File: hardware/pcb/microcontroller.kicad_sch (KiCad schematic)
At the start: 46 parts, among them J3 GT-USB-7010ASV, J5 helios-pinout, Q1 2N7002VC-, Q2 2N7002VC-, SW18 SWITCH, U3 USBLC6-2P6, U4 TLV74333PDBVR, U5 W25Q128JVPIQ, U6 RP2040, U7 74LVC1T45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

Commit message: Version 2 sent to production
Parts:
- removed C9: 15p, Capacitor_SMD:C_0402_1005Metric, symbol Device:C
- removed FB1: 600R, Resistor_SMD:R_0402_1005Metric, symbol Device:FerriteBead_Small
- removed U4: TLV74333PDBVR, Package_TO_SOT_SMD:SOT-23-5, symbol 0xcb:LP5907SNX-3.3-NOPB
- removed U5: W25Q128JVPIQ, Package_SO:SOIC-8W_5.3x5.3mm_P1.27mm, symbol 0xcb:W25Q128JVPIQ
- added C21: 4.7u, Capacitor_SMD:C_0402_1005Metric, symbol Device:C
- added U1: W25Q64JV, Package_SON:WSON-8-1EP_8x6mm_P1.27mm_EP3.4x4.3mm, symbol Mathboard:W25Q64JV
- added U4: XC6206P332MR-G, Package_TO_SOT_SMD:SOT-23, symbol Mathboard:XC6206P332MR-G
- C2, C4, C5: value 10u -> 4.7u; LCSC C15525 -> C23733; MPN  10uF 20% 10V 0402 -> 4.7uF 20% 10V 0402
- C6: value 10u -> 30p; footprint Capacitor_SMD:C_0402_1005Metric -> Capacitor_SMD:C_0603_1608Metric; LCSC C15525 -> C1658; MPN  10uF 20% 10V 0402 -> 0603CG300J500NT
- C8: value 15p -> 30p; footprint Capacitor_SMD:C_0402_1005Metric -> Capacitor_SMD:C_0603_1608Metric; LCSC C1548 -> C1658; MPN  15pF 5% 10V -> 0603CG300J500NT
- D17: value PMEG2010BELD -> DSL14; footprint Diode_SMD:D_SOD-882D -> Diode_SMD:D_SOD-123; JLCPCB_CORRECTION 0; 0; 180 -> (none); LCSC C552820 -> C22466349; MPN  PMEG2010BELD,315 -> DSL14
- J3: value GT-USB-7010ASV -> TYPE-C sinking plate; footprint mathboard:USB_C_Receptacle_G-Switch_GT-USB-7010ASV -> mathboard:USB_C_Receptacle_XYECONN TYPE-C-F02C-1BBWC1.6; LCSC C2988369 -> C20883026; MPN  USB4510-03-1-A -> TYPE-C-F02C-1BBWC1.6
- R12, R13: footprint Resistor_SMD:R_0402_1005Metric -> Resistor_SMD:R_0603_1608Metric; LCSC C25100 -> C25190
- Y1: LCSC C2149204 -> C9002; MPN  ECS-120-10-36B-CWY-TR3 -> X322512MSB4SI
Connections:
- net +3V3: now also C5.1, U1.8 (VCC), U4.2 (VOUT); no longer C6.1
- net +5V: now also C21.1, U4.3 (VIN); no longer C5.1
- net GND: now also C2.1, C6.1, J3.S1 (SHIELD), C21.2, U1.4 (GND), U1.9 (EP), U4.1 (VSS); no longer C2.2, C6.2
- net QSPI_CLK: now also U1.6 (CLK)
- net QSPI_CS: now also U1.1 (~{CS})
- net QSPI_SD0: now also U1.5 (DI(IO0))
- net QSPI_SD1: now also U1.2 (DO(IO1))
- net QSPI_SD2: now also U1.3 (IO2)
- net QSPI_SD3: now also U1.7 (IO3)
- net VBUS: now also C2.2; no longer C2.1
- net at R14.1, Y1.1: now also C6.2
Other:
- moved on the sheet: C7

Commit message: Revision 4
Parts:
- U1: footprint Package_SON:WSON-8-1EP_8x6mm_P1.27mm_EP3.4x4.3mm -> mathboard:WSON-8-1EP_8x6mm_P1.27mm_EP3.4x4.3mm
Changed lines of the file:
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@@
 			)
 		)
-		(property "Footprint" "Package_SON:WSON-8-1EP_8x6mm_P1.27mm_EP3.4x4.3mm"
+		(property "Footprint" "mathboard:WSON-8-1EP_8x6mm_P1.27mm_EP3.4x4.3mm"
 			(at 134.874 73.152 0)
 			(effects

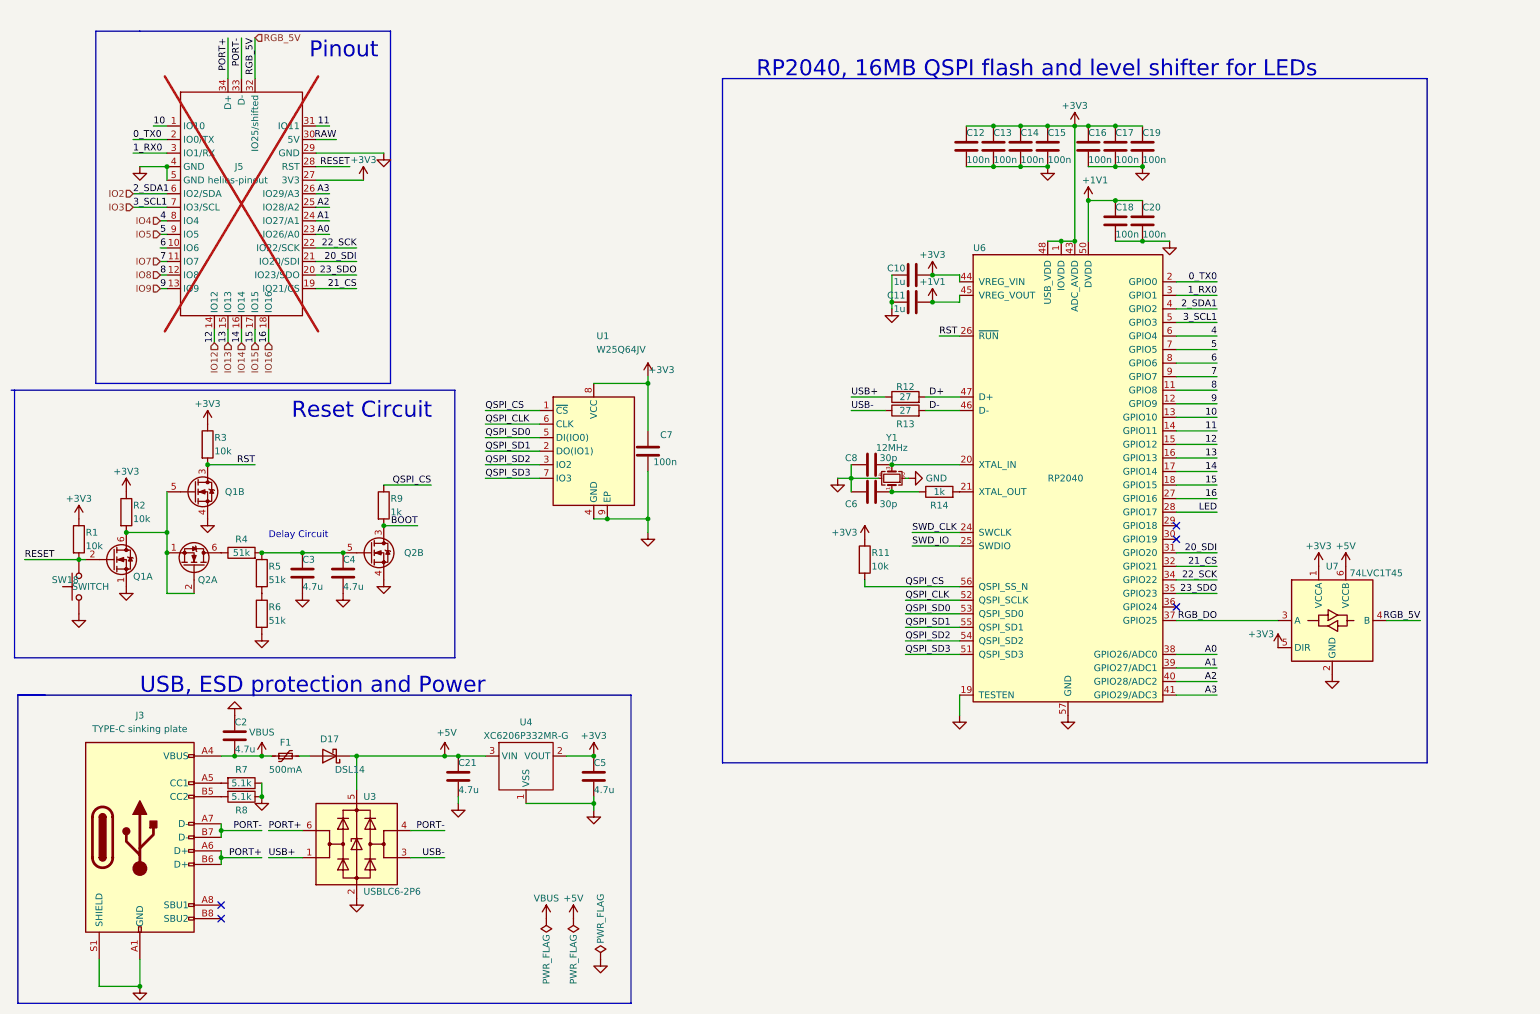
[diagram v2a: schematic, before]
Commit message: Added version encoder resistors
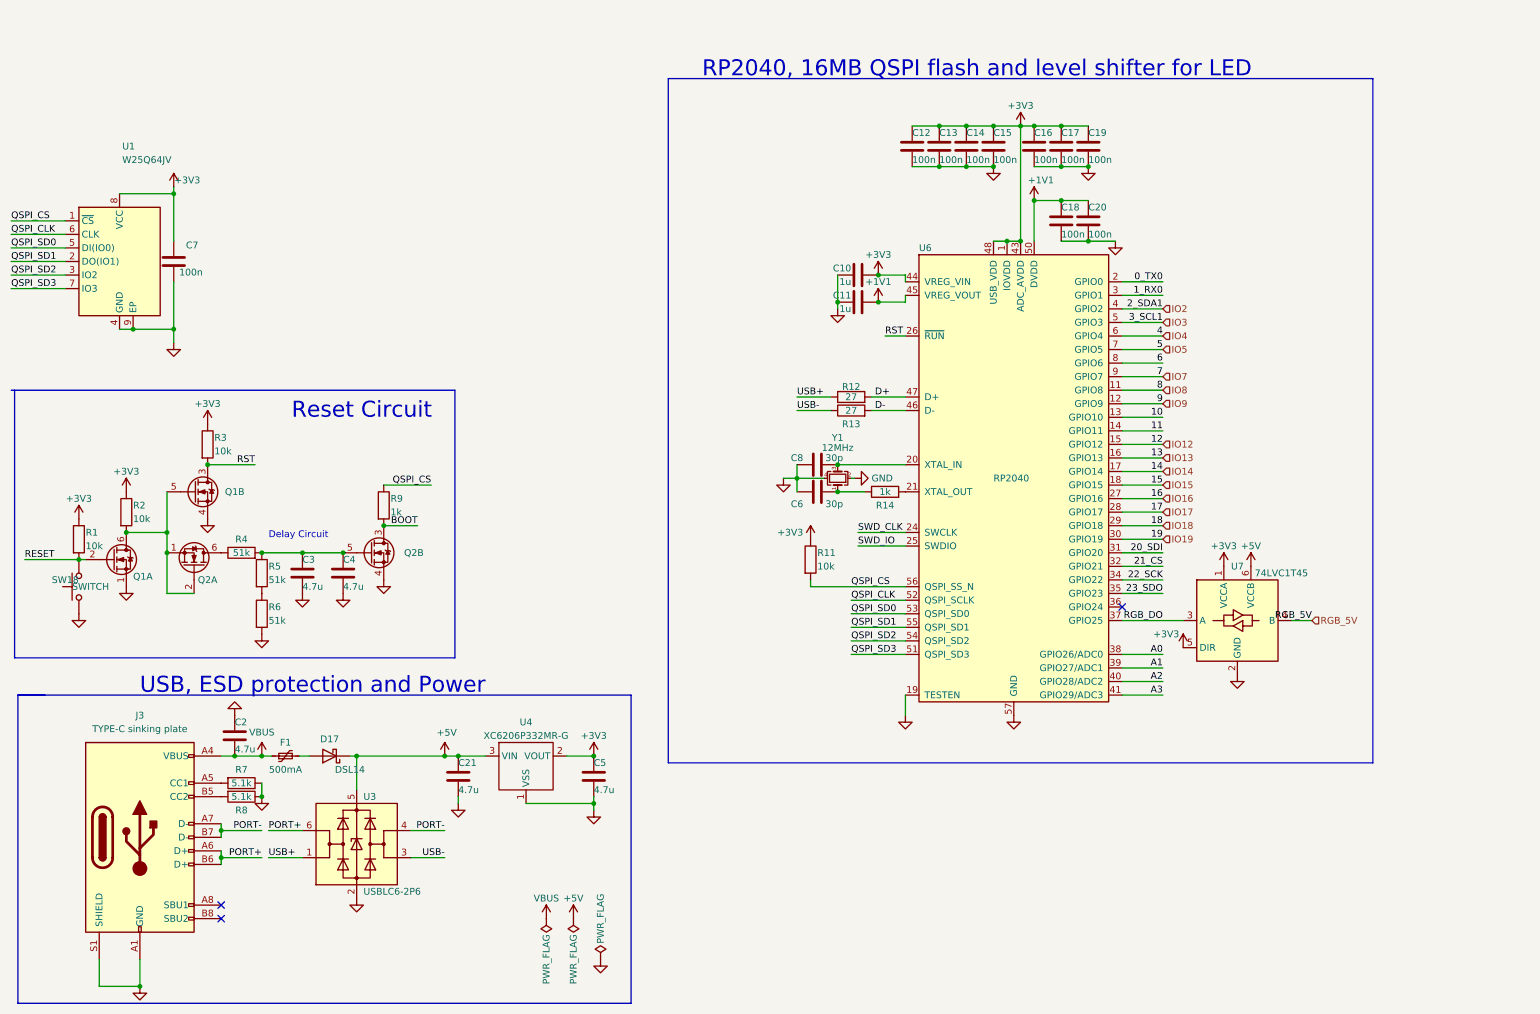
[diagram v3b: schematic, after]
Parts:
- removed J5: helios-pinout, 0xcb:helios, symbol 0xcb:helios-pinout
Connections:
- net IO18: now reaches U6.29 (GPIO18)
- net IO19: now reaches U6.30 (GPIO19)
- net LED renamed IO17
- no-connect marks 5 -> 3
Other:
- note added: "RP2040, 16MB QSPI flash and level shifter for LED"
- note removed: "Pinout"
- note removed: "RP2040, 16MB QSPI flash and level shifter for LEDs"
- moved on the sheet: C10, C11, C12, C13, C14, C15, C16, C17, C18, C19, C20, C6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

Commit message: Better EMC and ESD safety
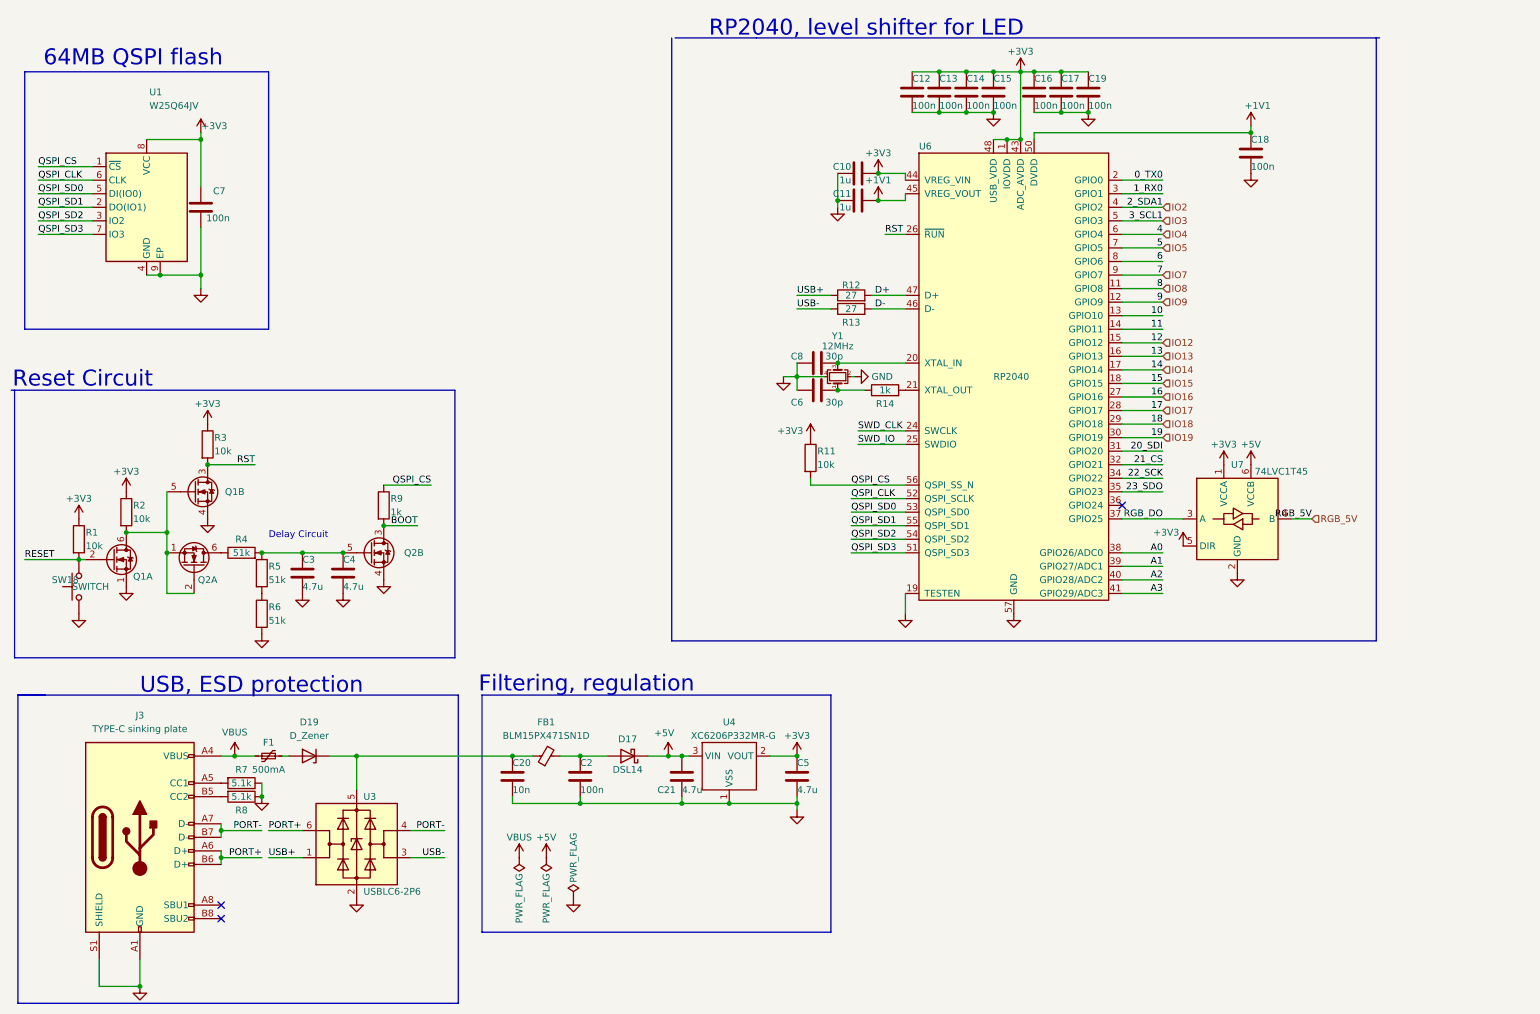
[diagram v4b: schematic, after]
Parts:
- added D19: D_Zener, mathboard:DFN1006-2L, symbol Device:D_Zener
- added FB1: BLM15PX471SN1D, Inductor_SMD:L_0402_1005Metric, symbol Device:FerriteBead_Small
- C2: value 4.7u -> 100n; LCSC C23733 -> C1525; MPN  4.7uF 20% 10V 0402 -> 100nF 10% 10V 0402
- C20: value 100n -> 10n; footprint Capacitor_SMD:C_0402_1005Metric -> Capacitor_SMD:C_0603_1608Metric; LCSC C1525 -> C282517; MPN  100nF 10% 10V 0402 -> 250V 10nF X7R ±10%
- C6, C8: LCSC C1658 -> C1658
- F1: footprint Fuse:Fuse_0603_1608Metric -> Fuse:Fuse_0402_1005Metric; LCSC C210357 -> C914085; MPN  MF-FSMF050X-2 -> BSMD0402L-020
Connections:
- net +1V1: no longer C20.1
- net +5V: no longer U3.5 (VBUS)
- net GND: now also C2.2; no longer C2.1
- net VBUS: no longer C2.2
- net at D17.2 (A): now also C2.1, FB1.2; no longer F1.2
- new net: C20.1, D19.1 (K), FB1.1, U3.5 (VBUS)
- new net: D19.2 (A), F1.2
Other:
- note added: "64MB QSPI flash"
- note added: "Filtering, regulation"
- note added: "RP2040, level shifter for LED"
- note added: "USB, ESD protection"
- note removed: "RP2040, 16MB QSPI flash and level shifter for LED"
- note removed: "USB, ESD protection and Power"
- moved on the sheet: C10, C11, C12, C13, C14, C15, C16, C17, C18, C19, C21, C5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

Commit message: Version 1.5
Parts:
- removed C2: 100n, Capacitor_SMD:C_0402_1005Metric, symbol Device:C
- removed C20: 10n, Capacitor_SMD:C_0603_1608Metric, symbol Device:C
- removed C21, C5: 4.7u, Capacitor_SMD:C_0402_1005Metric, symbol Device:C
- removed D17: DSL14, Diode_SMD:D_SOD-123, symbol Device:D_Schottky
- removed D19: D_Zener, mathboard:DFN1006-2L, symbol Device:D_Zener
- removed F1: 500mA, Fuse:Fuse_0402_1005Metric, symbol Device:Polyfuse_Small
- removed FB1: BLM15PX471SN1D, Inductor_SMD:L_0402_1005Metric, symbol Device:FerriteBead_Small
- removed J3: TYPE-C sinking plate, mathboard:USB_C_Receptacle_XYECONN TYPE-C-F02C-1BBWC1.6, symbol Connector:USB_C_Receptacle_USB2.0
- removed R7, R8: 5.1k, Resistor_SMD:R_0402_1005Metric, symbol Device:R
- removed U3: USBLC6-2P6, Package_TO_SOT_SMD:SOT-666, symbol Power_Protection:USBLC6-2P6
- removed U4: XC6206P332MR-G, Package_TO_SOT_SMD:SOT-23, symbol Mathboard:XC6206P332MR-G
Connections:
- no-connect marks 3 -> 1
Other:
- note removed: "Filtering, regulation"
- note removed: "USB, ESD protection"
- moved on the sheet: C10, C11, C12, C13, C14, C15, C16, C17, C18, C19, C3, C4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

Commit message: Remove old Mathboard kicad project
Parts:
- C3, C4: footprint Capacitor_SMD:C_0402_1005Metric -> Capacitor_SMD:C_0603_1608Metric; LCSC C23733 -> C1705
- SW18: footprint mathboard:SW_Push_1P1T_XKB_TS-1187A -> mathpad:SW_Push_1P1T_XKB_TS-1187A
- U1: footprint mathboard:WSON-8-1EP_8x6mm_P1.27mm_EP3.4x4.3mm -> Package_SON:WSON-8-1EP_8x6mm_P1.27mm_EP3.4x4.3mm; symbol Mathboard:W25Q64JV -> Mathpad:W25Q64JV
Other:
- company: (none) -> Summacogni OÜ
- title: (none) -> Mathpad
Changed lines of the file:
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@@
 	(generator_version "8.0")
 	(paper "A4")
+	(title_block
+		(title "Mathpad")
+		(date "2025-04-05")
+		(rev "1.6")
+		(company "Summacogni OÜ")
+	)
 	(junction
 		(at 162.56 66.04)
@@
 	)
 	(symbol
-		(lib_id "Mathboard:W25Q64JV")
+		(lib_id "Mathpad:W25Q64JV")
 		(at 63.5 62.23 0)
 		(unit 1)
@@
 			)
 		)
-		(property "Footprint" "mathboard:WSON-8-1EP_8x6mm_P1.27mm_EP3.4x4.3mm"
+		(property "Footprint" "Package_SON:WSON-8-1EP_8x6mm_P1.27mm_EP3.4x4.3mm"
 			(at 71.374 41.402 0)
 			(effects
@@
 			)
 		)
-		(property "Footprint" "Capacitor_SMD:C_0402_1005Metric"
+		(property "Footprint" "Capacitor_SMD:C_0603_1608Metric"
 			(at 96.2152 137.16 0)
 			(effects
@@
 			)
 		)
-		(property "LCSC" "C23733"
+		(property "LCSC" "C1705"
 			(at 95.25 133.35 0)
 			(effects
@@
 			)
 		)
-		(property "Footprint" "mathboard:SW_Push_1P1T_XKB_TS-1187A"
+		(property "Footprint" "mathpad:SW_Push_1P1T_XKB_TS-1187A"
 			(at 48.26 135.89 0)
 			(effects
@@
 			)
 		)
-		(property "Footprint" "Capacitor_SMD:C_0402_1005Metric"
+		(property "Footprint" "Capacitor_SMD:C_0603_1608Metric"
 			(at 103.8352 137.16 0)
 			(effects
@@
 			)
 		)
-		(property "LCSC" "C23733"
+		(property "LCSC" "C1705"
 			(at 102.87 133.35 0)
 			(effects
